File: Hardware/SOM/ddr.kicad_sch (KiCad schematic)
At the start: 0 parts

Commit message: SOM: +DDR IC
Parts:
- added C1, C2, C3, C4, C8, C9: 100nF, Capacitor_SMD:C_0402_1005Metric, symbol RA8M1:885012205092
- added C40, C41, C6, C7: 1uF, Capacitor_SMD:C_0402_1005Metric, symbol RA8M1:885012205092
- added C5, C67: 22uF, Capacitor_SMD:C_0805_2012Metric, symbol RA8M1:885012205092
- added L1, L2: 600R, Inductor_SMD:L_0402_1005Metric, symbol Device:L
- added U2: AS4C256M16D3, Package_BGA:BGA-96_9.0x13.0mm_Layout2x3x16_P0.8mm, symbol Memory_RAM:AS4C256M16D3
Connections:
- new net DDR_A0: U2.N3 (A0)
- new net DDR_A1: U2.P7 (A1)
- new net DDR_A10: U2.L7 (A10/AP)
- new net DDR_A11: U2.R7 (A11)
- new net DDR_A12: U2.N7 (A12/~{BC})
- new net DDR_A13: U2.T3 (A13)
- new net DDR_A14: U2.T7 (A14)
- new net DDR_A2: U2.P3 (A2)
- new net DDR_A3: U2.N2 (A3)
- new net DDR_A4: U2.P8 (A4)
- new net DDR_A5: U2.P2 (A5)
- new net DDR_A6: U2.R8 (A6)
- new net DDR_A7: U2.R2 (A7)
- new net DDR_A8: U2.T8 (A8)
- new net DDR_A9: U2.R3 (A9)
- new net DDR_BA0: U2.M2 (BA0)
- new net DDR_BA1: U2.N8 (BA1)
- new net DDR_BA2: U2.M3 (BA2)
- new net DDR_CAS: U2.K3 (~{CAS})
- new net DDR_CK: U2.J7 (CK)
- new net DDR_CKE: U2.K9 (CKE)
- new net DDR_CS: U2.L2 (~{CS})
- new net DDR_DQ0: U2.E3 (DQ0)
- new net DDR_DQ1: U2.F7 (DQ1)
- new net DDR_DQ10: U2.C8 (DQ10)
- new net DDR_DQ11: U2.C2 (DQ11)
- new net DDR_DQ12: U2.A7 (DQ12)
- new net DDR_DQ13: U2.A2 (DQ13)
- new net DDR_DQ14: U2.B8 (DQ14)
- new net DDR_DQ15: U2.A3 (DQ15)
- new net DDR_DQ2: U2.F2 (DQ2)
- new net DDR_DQ3: U2.F8 (DQ3)
- new net DDR_DQ4: U2.H3 (DQ4)
- new net DDR_DQ5: U2.H8 (DQ5)
- new net DDR_DQ6: U2.G2 (DQ6)
- new net DDR_DQ7: U2.H7 (DQ7)
- new net DDR_DQ8: U2.D7 (DQ8)
- new net DDR_DQ9: U2.C3 (DQ9)
- new net DDR_LDM: U2.E7 (LDM)
- new net DDR_LDQS: U2.F3 (LDQS)
- new net DDR_NCK: U2.K7 (~{CK})
- new net DDR_NLDQS: U2.G3 (~{LDQS})
- new net DDR_NUDQS: U2.B7 (~{UDQS})
- new net DDR_ODT: U2.K1 (ODT)
- new net DDR_RAS: U2.J3 (~{RAS})
- new net DDR_RST: U2.T2 (~{RESET})
- new net DDR_UDM: U2.D3 (UDM)
- new net DDR_UDQS: U2.C7 (UDQS)
- new net DDR_VDDQ_1.5V: C4.2, C5.2, C6.2, C7.2, C8.2, C9.2, L2.2, U2.A1 (VDDQ), U2.A8 (VDDQ), U2.C1 (VDDQ), U2.C9 (VDDQ), U2.D2 (VDDQ), U2.E9 (VDDQ), U2.F1 (VDDQ), U2.H2 (VDDQ), U2.H9 (VDDQ)
- new net DDR_VDD_1.5V: C1.2, C2.2, C3.2, C40.2, C41.2, C67.2, L1.2, U2.B2 (VDD), U2.D9 (VDD), U2.G7 (VDD), U2.K2 (VDD), U2.K8 (VDD), U2.N1 (VDD), U2.N9 (VDD), U2.R1 (VDD), U2.R9 (VDD)
- new net DDR_VREF: U2.H1 (VREFDQ), U2.M8 (VREFCA)
- new net DDR_WE: U2.L3 (~{WE})
- new net DDR_ZQ: U2.L8 (ZQ)
- new net GND: C1.1, C2.1, C3.1, C4.1, C40.1, C41.1, C5.1, C6.1, C67.1, C7.1, C8.1, C9.1, U2.A9 (VSS), U2.B1 (VSSQ), U2.B3 (VSS), U2.B9 (VSSQ), U2.D1 (VSSQ), U2.D8 (VSSQ), U2.E1 (VSS), U2.E2 (VSSQ), U2.E8 (VSSQ), U2.F9 (VSSQ), U2.G1 (VSSQ), U2.G8 (VSS), U2.G9 (VSSQ), U2.J2 (VSS), U2.J8 (VSS), U2.M1 (VSS), U2.M9 (VSS), U2.P1 (VSS), U2.P9 (VSS), U2.T1 (VSS), U2.T9 (VSS)
- new net VDD_1.5V: L1.1, L2.1
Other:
- note added: "DDR"
- note added: "DDR Power"

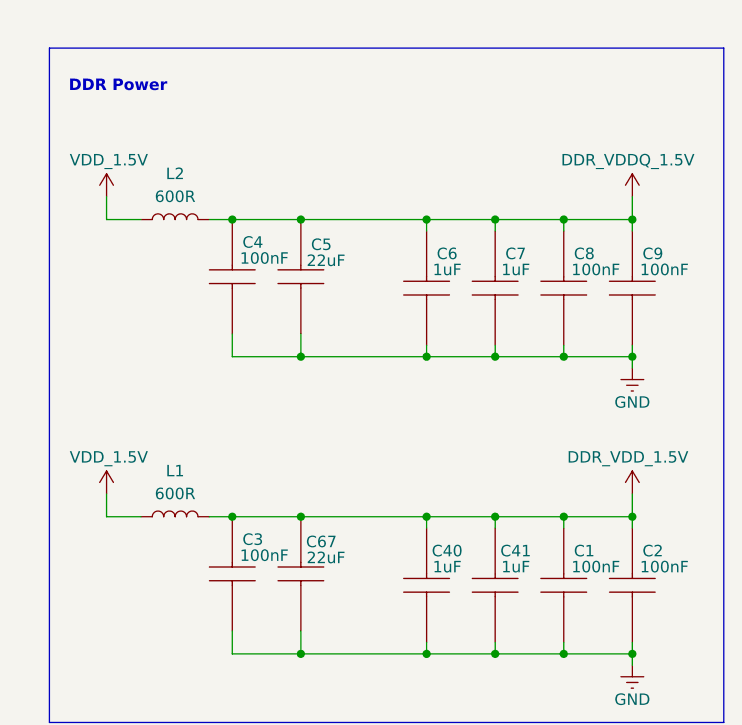
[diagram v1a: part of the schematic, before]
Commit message: SOM: SO-DIMM connector
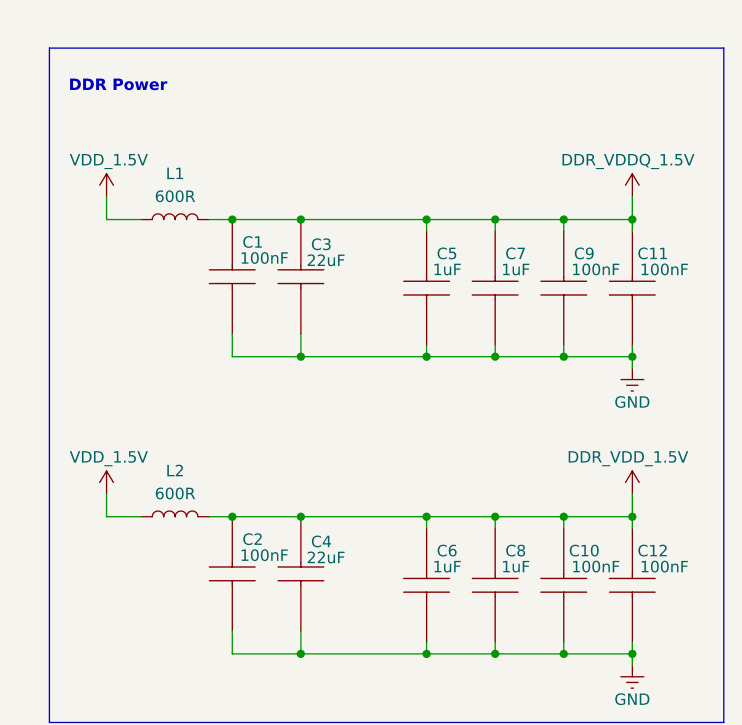
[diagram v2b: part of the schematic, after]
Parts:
- renumbered C4 to C1, C1 to C10, C9 to C11, C2 to C12, C3 to C2, C5 to C3, C67 to C4, C6 to C5, C40 to C6, C41 to C8, C8 to C9, L2 to L1, L1 to L2
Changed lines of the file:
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@@
 		(on_board yes)
 		(dnp no)
-		(property "Reference" "C4"
+		(property "Reference" "C1"
 			(at 210.566 72.39 90)
 			(effects
@@
 			(project "LFE5UM5G-85F_SOM"
 				(path "/de32abb0-ff3b-4c67-a91a-eed08140b1b2/70285655-daa5-4a1b-b29b-80c93a345d65"
-					(reference "C4")
+					(reference "C1")
 					(unit 1)
 				)
@@
 		(on_board yes)
 		(dnp no)
-		(property "Reference" "C8"
+		(property "Reference" "C9"
 			(at 247.396 73.66 90)
 			(effects
@@
 			(project "LFE5UM5G-85F_SOM"
 				(path "/de32abb0-ff3b-4c67-a91a-eed08140b1b2/70285655-daa5-4a1b-b29b-80c93a345d65"
-					(reference "C8")
+					(reference "C9")
 					(unit 1)
 				)
@@
 		(on_board yes)
 		(dnp no)
-		(property "Reference" "C40"
+		(property "Reference" "C6"
 			(at 232.156 106.68 90)
 			(effects
@@
 			(project "LFE5UM5G-85F_SOM"
 				(path "/de32abb0-ff3b-4c67-a91a-eed08140b1b2/70285655-daa5-4a1b-b29b-80c93a345d65"
-					(reference "C40")
+					(reference "C6")
 					(unit 1)
 				)
@@
 		(on_board yes)
 		(dnp no)
-		(property "Reference" "C1"
+		(property "Reference" "C10"
 			(at 247.396 106.68 90)
 			(effects
@@
 			(project "LFE5UM5G-85F_SOM"
 				(path "/de32abb0-ff3b-4c67-a91a-eed08140b1b2/70285655-daa5-4a1b-b29b-80c93a345d65"
-					(reference "C1")
+					(reference "C10")
 					(unit 1)
 				)
@@
 		(dnp no)
 		(fields_autoplaced yes)
-		(property "Reference" "#PWR03"
+		(property "Reference" "#PWR02"
 			(at 95.25 149.86 0)
 			(effects
@@
 		)
 		(instances
-			(project ""
-				(path "/de32abb0-ff3b-4c67-a91a-eed08140b1b2/70285655-daa5-4a1b-b29b-80c93a345d65"
-					(reference "#PWR03")
+			(project "LFE5UM5G-85F_SOM"
+				(path "/de32abb0-ff3b-4c67-a91a-eed08140b1b2/70285655-daa5-4a1b-b29b-80c93a345d65"
+					(reference "#PWR02")
 					(unit 1)
 				)
@@
 		(dnp no)
 		(fields_autoplaced yes)
-		(property "Reference" "L1"
+		(property "Reference" "L2"
 			(at 201.93 97.79 90)
 			(effects
@@
 		)
 		(instances
-			(project ""
-				(path "/de32abb0-ff3b-4c67-a91a-eed08140b1b2/70285655-daa5-4a1b-b29b-80c93a345d65"
-					(reference "L1")
+			(project "LFE5UM5G-85F_SOM"
+				(path "/de32abb0-ff3b-4c67-a91a-eed08140b1b2/70285655-daa5-4a1b-b29b-80c93a345d65"
+					(reference "L2")
 					(unit 1)
 				)
@@
 		(on_board yes)
 		(dnp no)
-		(property "Reference" "C9"
+		(property "Reference" "C11"
 			(at 255.016 73.66 90)
 			(effects
@@
 			(project "LFE5UM5G-85F_SOM"
 				(path "/de32abb0-ff3b-4c67-a91a-eed08140b1b2/70285655-daa5-4a1b-b29b-80c93a345d65"
-					(reference "C9")
+					(reference "C11")
 					(unit 1)
 				)
@@
 		(on_board yes)
 		(dnp no)
-		(property "Reference" "C5"
+		(property "Reference" "C3"
 			(at 218.186 72.644 90)
 			(effects
@@
 			(project "LFE5UM5G-85F_SOM"
 				(path "/de32abb0-ff3b-4c67-a91a-eed08140b1b2/70285655-daa5-4a1b-b29b-80c93a345d65"
-					(reference "C5")
+					(reference "C3")
 					(unit 1)
 				)
@@
 		(on_board yes)
 		(dnp no)
-		(property "Reference" "C3"
+		(property "Reference" "C2"
 			(at 210.566 105.41 90)
 			(effects
@@
 			(project "LFE5UM5G-85F_SOM"
 				(path "/de32abb0-ff3b-4c67-a91a-eed08140b1b2/70285655-daa5-4a1b-b29b-80c93a345d65"
-					(reference "C3")
+					(reference "C2")
 					(unit 1)
 				)
@@
 		(on_board yes)
 		(dnp no)
-		(property "Reference" "#PWR04"
+		(property "Reference" "#PWR08"
 			(at 252.73 104.14 0)
 			(effects
@@
 			(project "LFE5UM5G-85F_SOM"
 				(path "/de32abb0-ff3b-4c67-a91a-eed08140b1b2/70285655-daa5-4a1b-b29b-80c93a345d65"
-					(reference "#PWR04")
+					(reference "#PWR08")
 					(unit 1)
 				)
@@
 		(on_board yes)
 		(dnp no)
-		(property "Reference" "#PWR08"
+		(property "Reference" "#PWR07"
 			(at 252.73 92.71 0)
 			(effects
@@
 			(project "LFE5UM5G-85F_SOM"
 				(path "/de32abb0-ff3b-4c67-a91a-eed08140b1b2/70285655-daa5-4a1b-b29b-80c93a345d65"
-					(reference "#PWR08")
+					(reference "#PWR07")
 					(unit 1)
 				)
@@
 		)
 		(instances
-			(project ""
+			(project "LFE5UM5G-85F_SOM"
 				(path "/de32abb0-ff3b-4c67-a91a-eed08140b1b2/70285655-daa5-4a1b-b29b-80c93a345d65"
 					(reference "#PWR01")
@@
 		(on_board yes)
 		(dnp no)
-		(property "Reference" "#PWR06"
+		(property "Reference" "#PWR04"
 			(at 194.31 71.12 0)
 			(effects
@@
 			(project "LFE5UM5G-85F_SOM"
 				(path "/de32abb0-ff3b-4c67-a91a-eed08140b1b2/70285655-daa5-4a1b-b29b-80c93a345d65"
-					(reference "#PWR06")
+					(reference "#PWR04")
 					(unit 1)
 				)
@@
 		(on_board yes)
 		(dnp no)
-		(property "Reference" "C2"
+		(property "Reference" "C12"
 			(at 255.016 106.68 90)
 			(effects
@@
 			(project "LFE5UM5G-85F_SOM"
 				(path "/de32abb0-ff3b-4c67-a91a-eed08140b1b2/70285655-daa5-4a1b-b29b-80c93a345d65"
-					(reference "C2")
+					(reference "C12")
 					(unit 1)
 				)
@@
 		(on_board yes)
 		(dnp no)
-		(property "Reference" "#PWR07"
+		(property "Reference" "#PWR06"
 			(at 252.73 71.12 0)
 			(effects
@@
 			(project "LFE5UM5G-85F_SOM"
 				(path "/de32abb0-ff3b-4c67-a91a-eed08140b1b2/70285655-daa5-4a1b-b29b-80c93a345d65"
-					(reference "#PWR07")
+					(reference "#PWR06")
 					(unit 1)
 				)
@@
 		)
 		(instances
-			(project ""
+			(project "LFE5UM5G-85F_SOM"
 				(path "/de32abb0-ff3b-4c67-a91a-eed08140b1b2/70285655-daa5-4a1b-b29b-80c93a345d65"
 					(reference "U2")
@@
 		(on_board yes)
 		(dnp no)
-		(property "Reference" "C67"
+		(property "Reference" "C4"
 			(at 218.186 105.664 90)
 			(effects
@@
 			(project "LFE5UM5G-85F_SOM"
 				(path "/de32abb0-ff3b-4c67-a91a-eed08140b1b2/70285655-daa5-4a1b-b29b-80c93a345d65"
-					(reference "C67")
+					(reference "C4")
 					(unit 1)
 				)
@@
 		(on_board yes)
 		(dnp no)
-		(property "Reference" "#PWR058"
+		(property "Reference" "#PWR09"
 			(at 252.73 125.73 0)
 			(effects
@@
 			(project "LFE5UM5G-85F_SOM"
 				(path "/de32abb0-ff3b-4c67-a91a-eed08140b1b2/70285655-daa5-4a1b-b29b-80c93a345d65"
-					(reference "#PWR058")
+					(reference "#PWR09")
 					(unit 1)
 				)
@@
 		(dnp no)
 		(fields_autoplaced yes)
-		(property "Reference" "L2"
+		(property "Reference" "L1"
 			(at 201.93 64.77 90)
 			(effects
@@
 			(project "LFE5UM5G-85F_SOM"
 				(path "/de32abb0-ff3b-4c67-a91a-eed08140b1b2/70285655-daa5-4a1b-b29b-80c93a345d65"
-					(reference "L2")
+					(reference "L1")
 					(unit 1)
 				)
@@
 		(on_board yes)
 		(dnp no)
-		(property "Reference" "C6"
+		(property "Reference" "C5"
 			(at 232.156 73.66 90)
 			(effects
@@
 			(project "LFE5UM5G-85F_SOM"
 				(path "/de32abb0-ff3b-4c67-a91a-eed08140b1b2/70285655-daa5-4a1b-b29b-80c93a345d65"
-					(reference "C6")
+					(reference "C5")
 					(unit 1)
 				)
@@
 		(on_board yes)
 		(dnp no)
-		(property "Reference" "#PWR02"
+		(property "Reference" "#PWR03"
 			(at 105.41 46.99 0)
 			(effects
@@
 			(project "LFE5UM5G-85F_SOM"
 				(path "/de32abb0-ff3b-4c67-a91a-eed08140b1b2/70285655-daa5-4a1b-b29b-80c93a345d65"
-					(reference "#PWR02")
+					(reference "#PWR03")
 					(unit 1)
 				)
@@
 		(on_board yes)
 		(dnp no)
-		(property "Reference" "C41"
+		(property "Reference" "C8"
 			(at 239.776 106.68 90)
 			(effects
@@
 			(project "LFE5UM5G-85F_SOM"
 				(path "/de32abb0-ff3b-4c67-a91a-eed08140b1b2/70285655-daa5-4a1b-b29b-80c93a345d65"
-					(reference "C41")
-					(unit 1)
-				)
+					(reference "C8")
+					(unit 1)
+				)

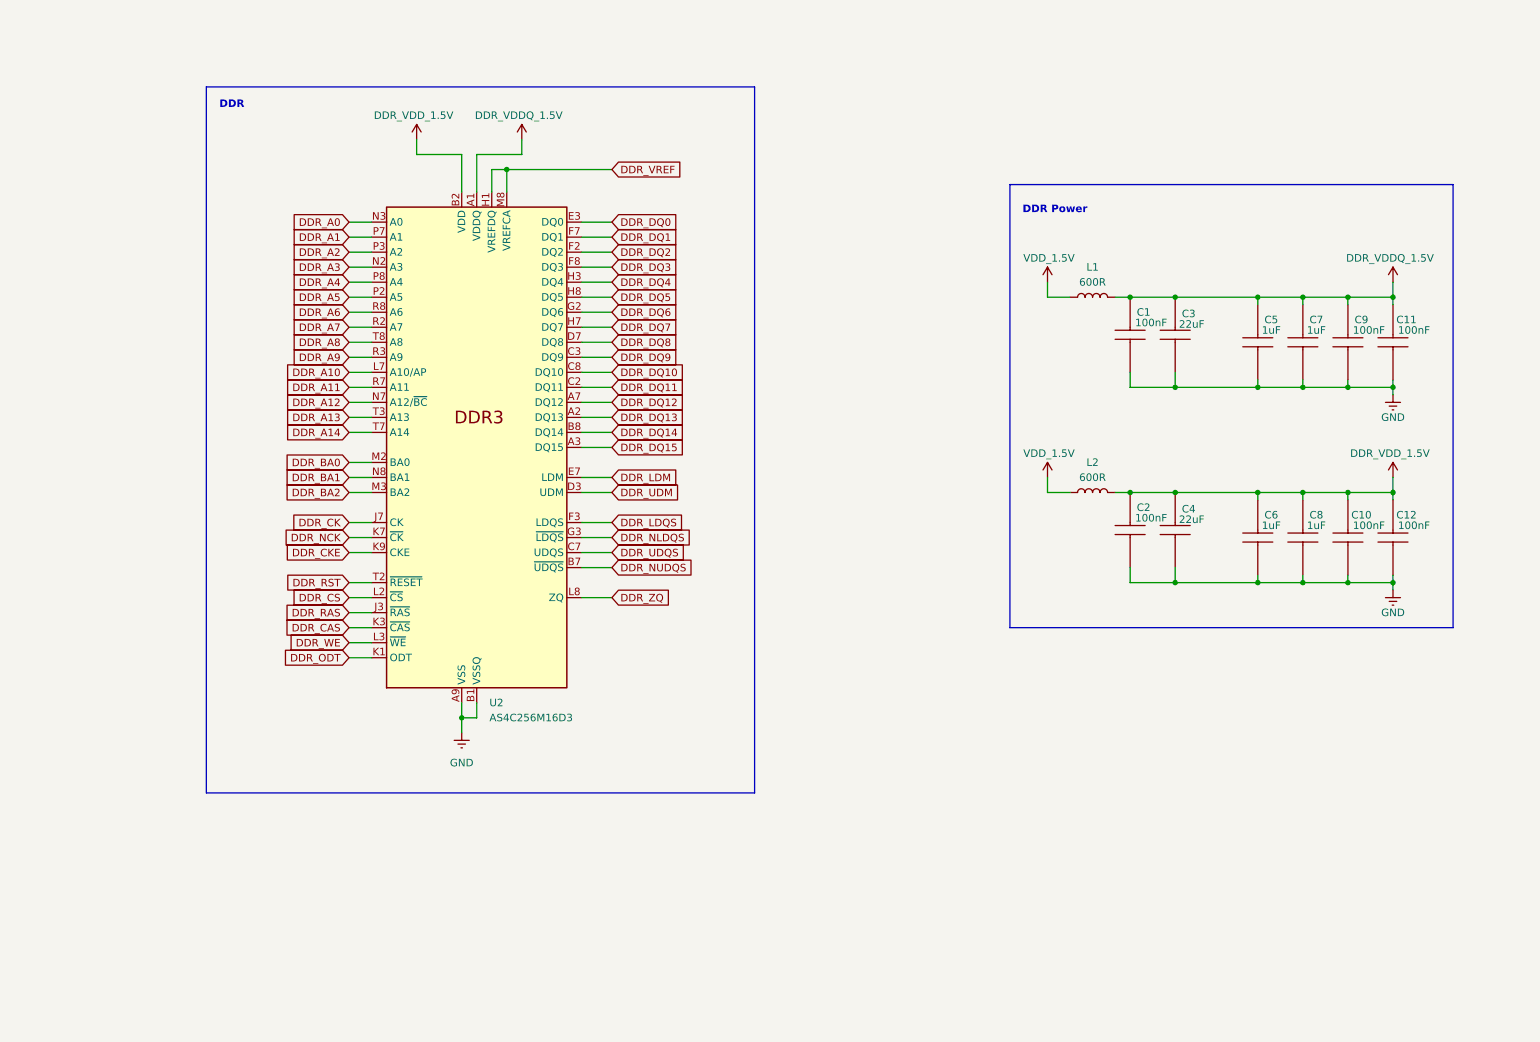
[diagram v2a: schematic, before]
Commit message: SOM: DDR schematics update
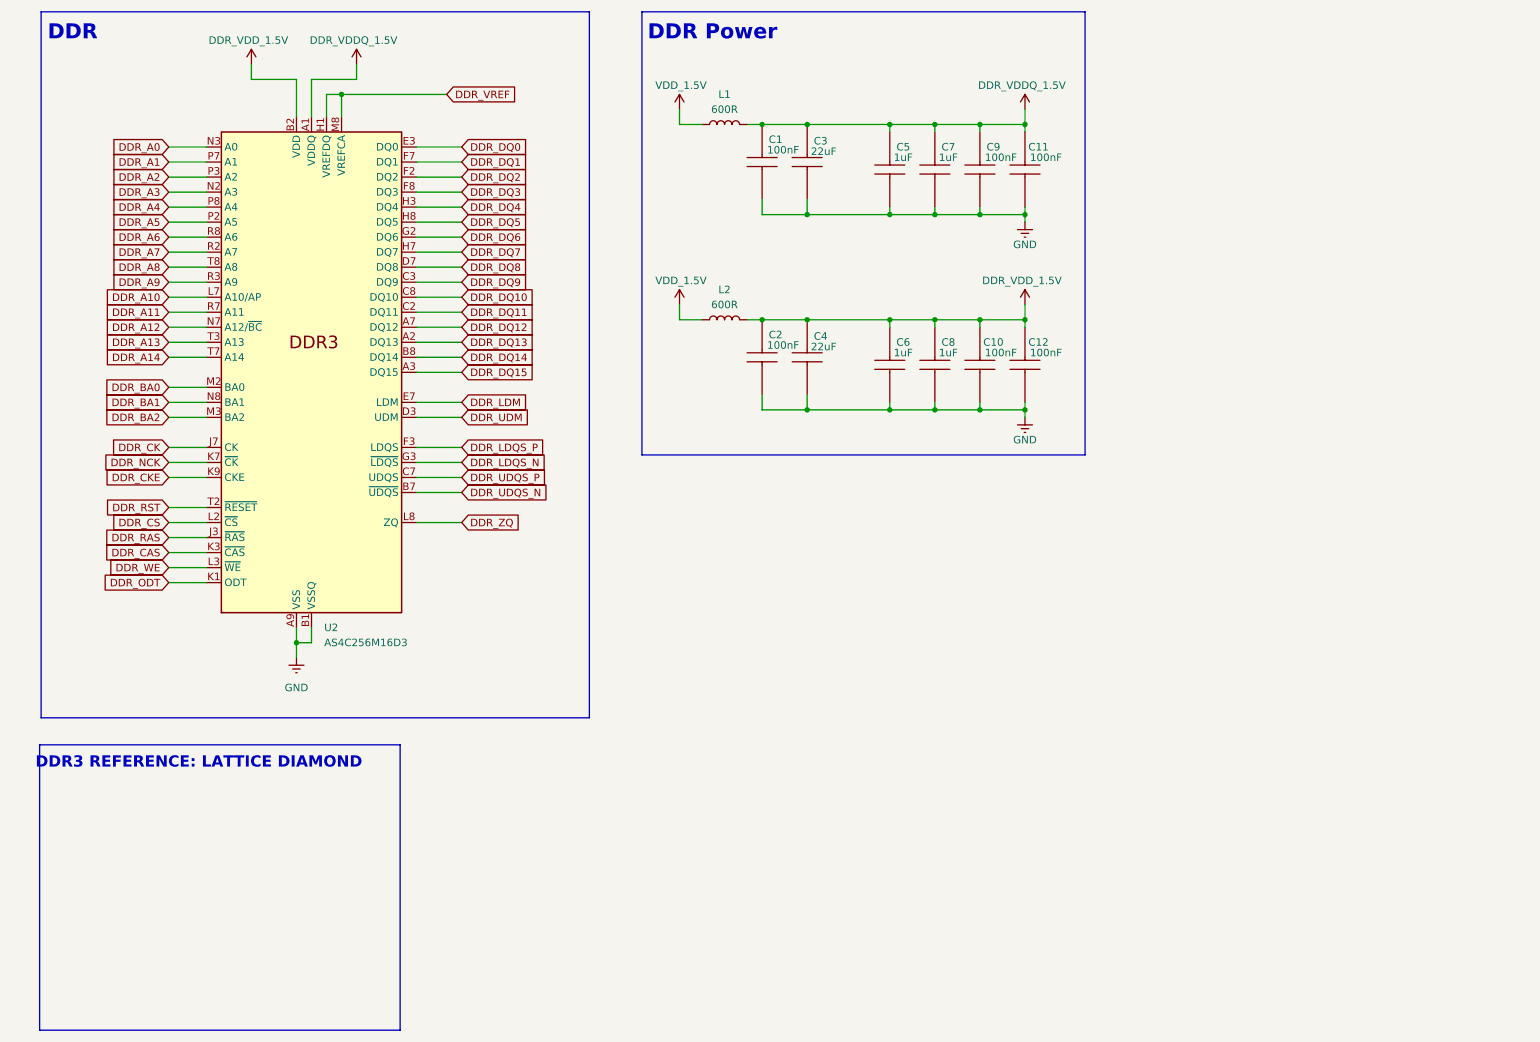
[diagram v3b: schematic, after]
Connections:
- net DDR_LDQS renamed DDR_LDQS_P
- net DDR_NLDQS renamed DDR_LDQS_N
- net DDR_NUDQS renamed DDR_UDQS_N
- net DDR_UDQS renamed DDR_UDQS_P
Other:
- note added: "DDR3 REFERENCE: LATTICE DIAMOND"
- moved on the sheet: C1, C10, C11, C12, C2, C3, C4, C5, C6, C7, C8, C9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
